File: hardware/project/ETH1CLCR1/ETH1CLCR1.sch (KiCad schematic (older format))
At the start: 0 parts

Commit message: Changes in schematics.
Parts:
- added M101: 60817-096, ETH1CLCR1:60817-096, symbol ETH1CLCR1:60817-096
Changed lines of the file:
@@
 S 2350 8200 1100 1500
 U 5E314C16
-F0 "FGEN Buffer" 50
+F0 "FGEN Buffer + Source resistor" 50
 F1 "FGEN_Buffer.sch" 50
 F2 "FGEN" I R 3450 9500 50
@@
 Wire Wire Line
 	11500 2350 12250 2350
+$Comp
+L ETH1CLCR1:60817-096 M101
+U 1 1 5E5B3C06
+P 800 10700
+F 0 "M101" H 1128 11046 50  0000 L CNN
+F 1 "60817-096" H 1128 10955 50  0000 L CNN
+F 2 "ETH1CLCR1:60817-096" H 800 10700 50  0001 C CNN
+F 3 "" H 800 10700 50  0001 C CNN
+	1    800  10700
+	1    0    0    -1
+$EndComp
 $EndSCHEMATC

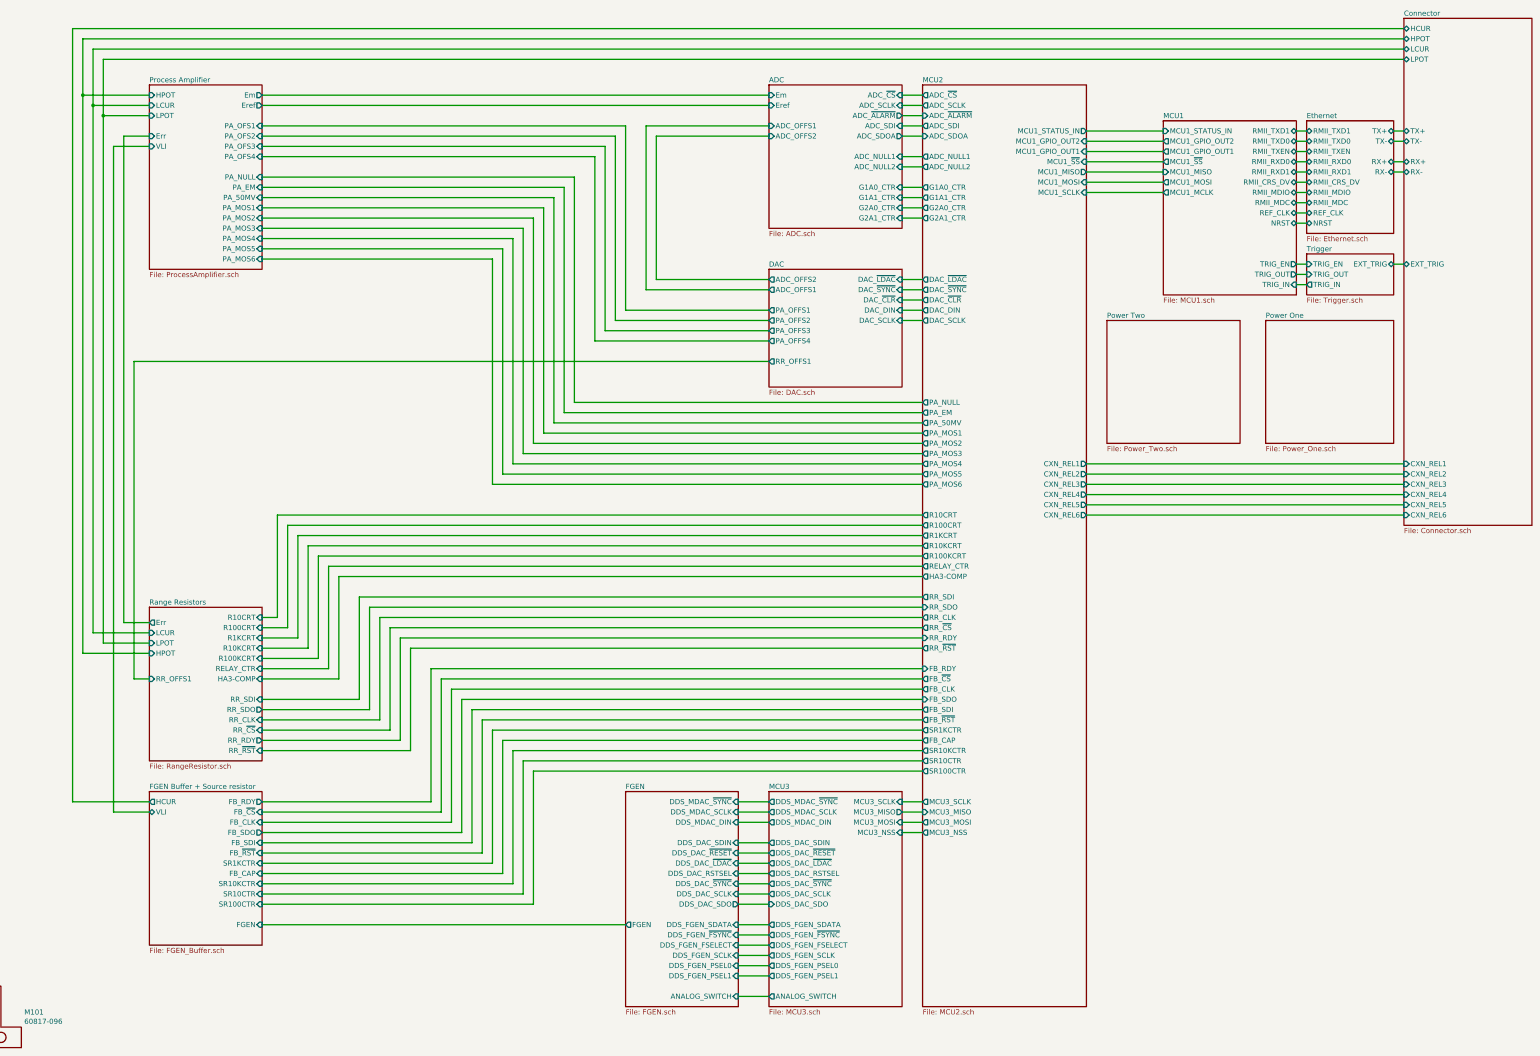
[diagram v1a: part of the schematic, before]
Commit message: Checked the schematics. Created BOM.
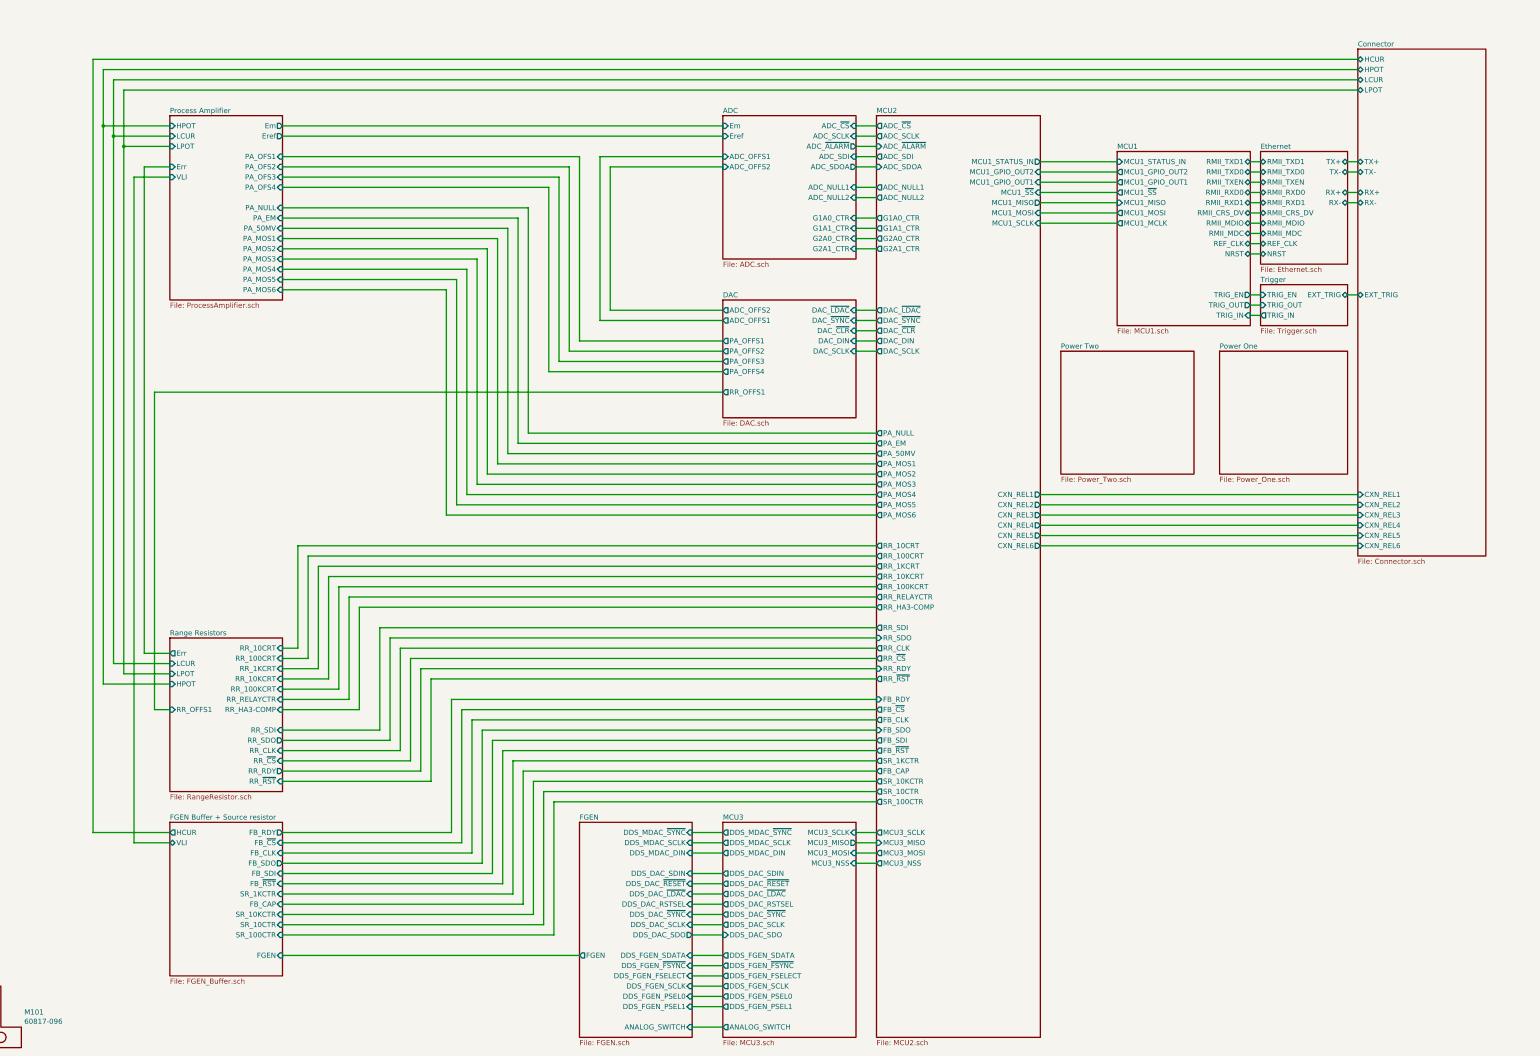
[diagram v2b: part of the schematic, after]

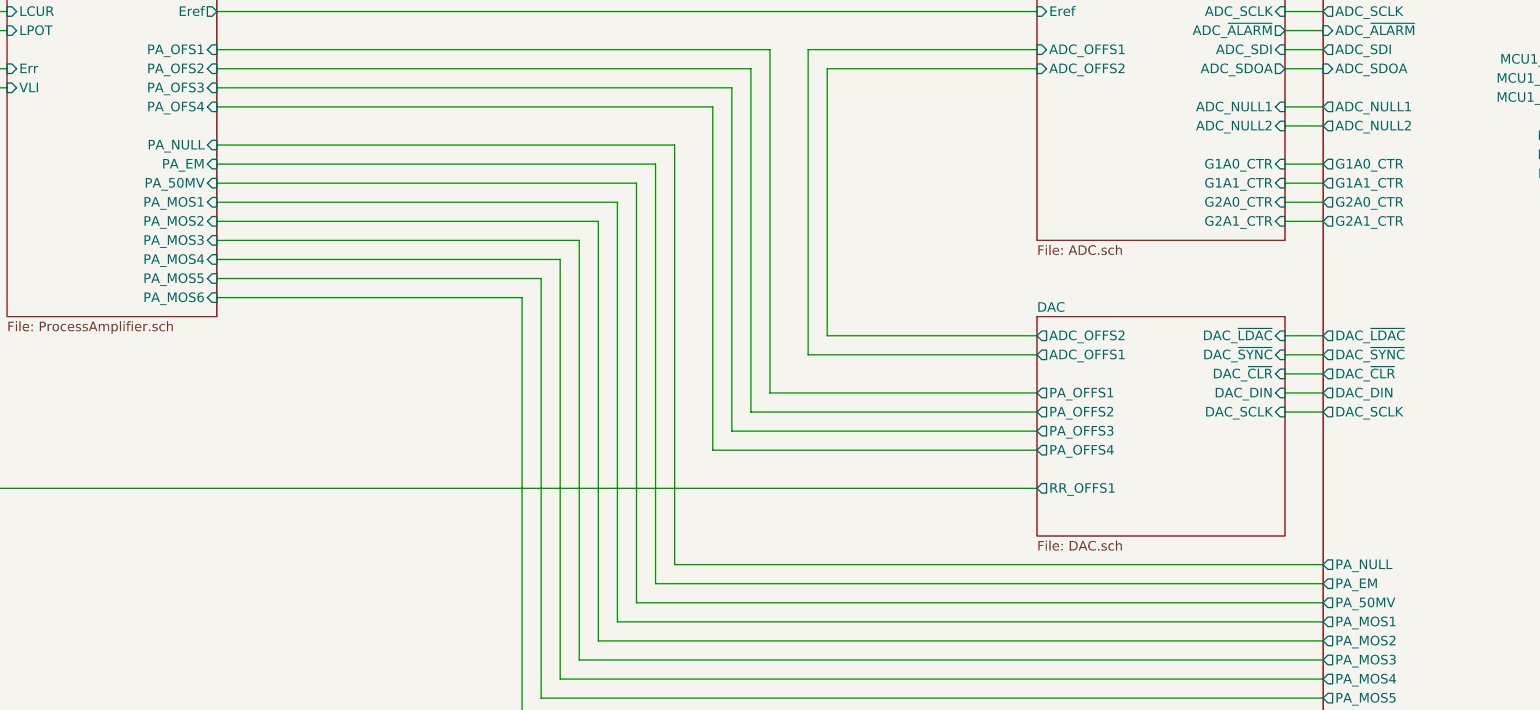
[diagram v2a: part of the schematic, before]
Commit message: Fixed some mistakes in the foorpeints. BOM list ready.
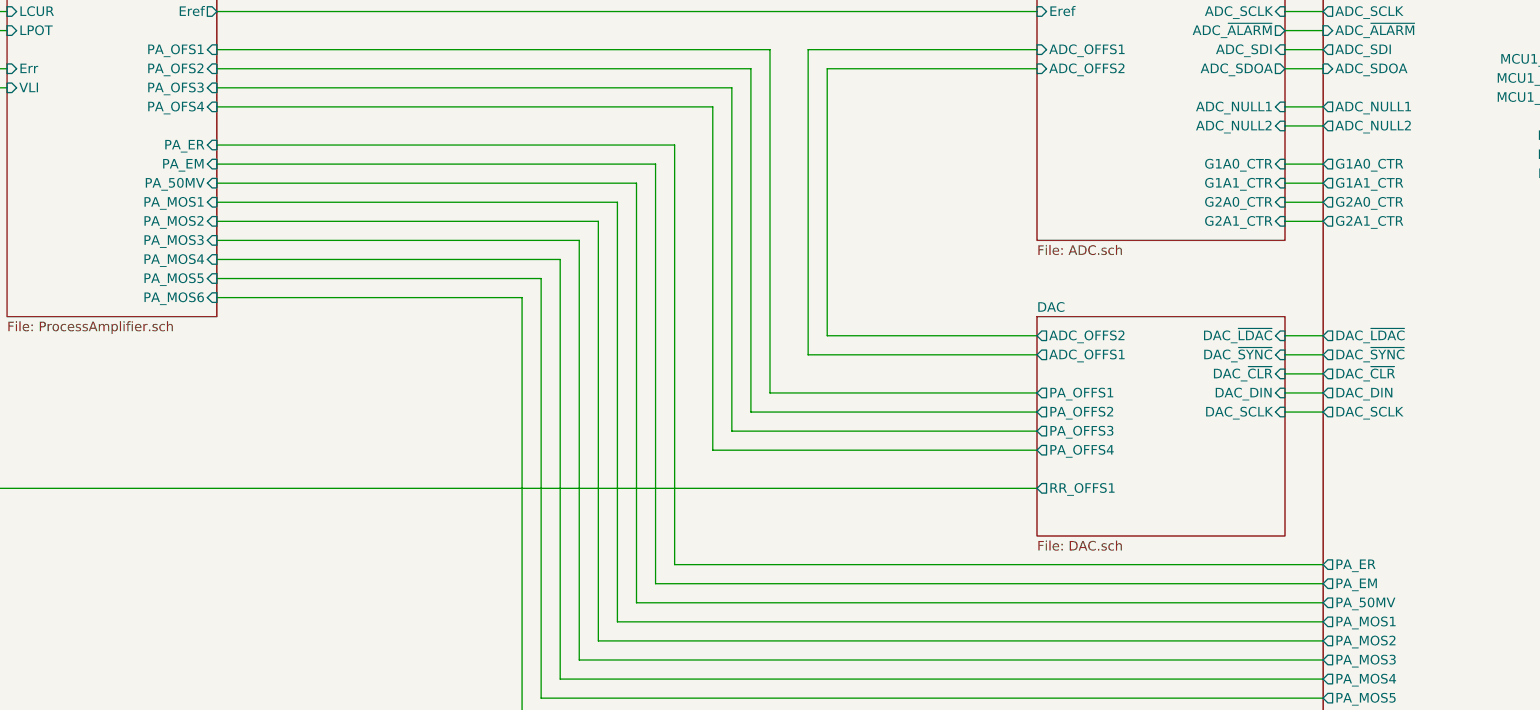
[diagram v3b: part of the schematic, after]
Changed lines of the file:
@@
 F11 "Eref" O R 3650 1800 50
 F12 "LPOT" I L 2550 1900 50
-F13 "PA_NULL" I R 3650 2500 50
+F13 "PA_ER" I R 3650 2500 50
 F14 "PA_EM" I R 3650 2600 50
 F15 "PA_50MV" I R 3650 2700 50
@@
 F18 "RR_RELAYCTR" O L 9450 6300 50
 F19 "RR_HA3-COMP" O L 9450 6400 50
-F20 "PA_NULL" O L 9450 4700 50
+F20 "PA_ER" O L 9450 4700 50
 F21 "PA_EM" O L 9450 4800 50
 F22 "PA_50MV" O L 9450 4900 50

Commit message: PCB layout
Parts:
- removed M101: 60817-096, ETH1CLCR1:60817-096, symbol ETH1CLCR1:60817-096
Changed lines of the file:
@@
 Wire Wire Line
 	11050 2650 11800 2650
-$Comp
-L ETH1CLCR1:60817-096 M101
-U 1 1 5E5B3C06
-P 800 10700
-F 0 "M101" H 1128 11046 50  0000 L CNN
-F 1 "60817-096" H 1128 10955 50  0000 L CNN
-F 2 "ETH1CLCR1:60817-096" H 800 10700 50  0001 C CNN
-F 3 "" H 800 10700 50  0001 C CNN
-	1    800  10700
-	1    0    0    -1
-$EndComp
 Wire Wire Line
 	1800 8600 2550 8600

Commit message: PCB layout
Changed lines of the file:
@@
 F13 "TRIG_OUT" O R 13100 3450 50
 F14 "TRIG_IN" I R 13100 3550 50
-F15 "MCU1_STATUS_IN" I L 11800 2050 50
-F16 "MCU1_GPIO_OUT2" O L 11800 2150 50
-F17 "MCU1_GPIO_OUT1" O L 11800 2250 50
-F18 "MCU1_~SS" O L 11800 2350 50
-F19 "MCU1_MISO" I L 11800 2450 50
-F20 "MCU1_MOSI" O L 11800 2550 50
-F21 "MCU1_MCLK" O L 11800 2650 50
+F15 "MCU1_GPIO_OUT2" O L 11800 2050 50
+F16 "MCU1_GPIO_OUT1" O L 11800 2150 50
+F17 "MCU1_~SS" O L 11800 2250 50
+F18 "MCU1_MISO" I L 11800 2350 50
+F19 "MCU1_MOSI" O L 11800 2450 50
+F20 "MCU1_MCLK" O L 11800 2550 50
+F21 "MCU1_STATUS_IN1" I L 11800 2650 50
+F22 "MCU1_STATUS_IN2" I L 11800 2750 50
 $EndSheet
 $Sheet
@@
 F59 "ADC_~ALARM" I L 9450 1900 50
 F60 "ADC_SDOA" I L 9450 2100 50
-F61 "MCU1_~SS" I R 11050 2350 50
-F62 "MCU1_MISO" O R 11050 2450 50
-F63 "MCU1_MOSI" I R 11050 2550 50
-F64 "MCU1_SCLK" I R 11050 2650 50
-F65 "MCU1_GPIO_OUT1" I R 11050 2250 50
-F66 "MCU1_STATUS_IN" O R 11050 2050 50
-F67 "MCU1_GPIO_OUT2" I R 11050 2150 50
+F61 "MCU1_~SS" I R 11050 2250 50
+F62 "MCU1_MISO" O R 11050 2350 50
+F63 "MCU1_MOSI" I R 11050 2450 50
+F64 "MCU1_SCLK" I R 11050 2550 50
+F65 "MCU1_GPIO_OUT1" I R 11050 2150 50
+F66 "MCU1_STATUS_IN1" O R 11050 2650 50
+F67 "MCU1_GPIO_OUT2" I R 11050 2050 50
+F68 "MCU1_STATUS_IN2" O R 11050 2750 50
 $EndSheet
 Wire Wire Line
@@
 $EndSheet
 Wire Wire Line
-	11050 2050 11800 2050
-Wire Wire Line
-	11050 2150 11800 2150
-Wire Wire Line
-	11050 2250 11800 2250
-Wire Wire Line
-	11050 2350 11800 2350
-Wire Wire Line
-	11050 2450 11800 2450
-Wire Wire Line
-	11050 2550 11800 2550
-Wire Wire Line
-	11050 2650 11800 2650
-Wire Wire Line
 	1800 8600 2550 8600
 Wire Wire Line
@@
 Wire Wire Line
 	2300 6850 2300 2100
+Wire Wire Line
+	11050 2550 11800 2550
+Wire Wire Line
+	11050 2450 11800 2450
+Wire Wire Line
+	11050 2350 11800 2350
+Wire Wire Line
+	11050 2250 11800 2250
+Wire Wire Line
+	11050 2150 11800 2150
+Wire Wire Line
+	11050 2050 11800 2050
+Wire Wire Line
+	11050 2650 11800 2650
+Wire Wire Line
+	11050 2750 11800 2750
 $EndSCHEMATC

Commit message: Was able to set the SPI3 (MCU2) to run with 80 MHZ clock speed with AD7380. Using HAL lib for SPI and GPIO, too slow switching. Need to change to LL with DMA.
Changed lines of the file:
@@
 F0 "Range Resistors" 50
 F1 "RangeResistor.sch" 50
-F2 "RR_1KCRT" I R 3650 7000 50
-F3 "RR_10KCRT" I R 3650 7100 50
-F4 "RR_100CRT" I R 3650 6900 50
-F5 "RR_10CRT" I R 3650 6800 50
-F6 "RR_100KCRT" I R 3650 7200 50
+F2 "RR_1KCTR" I R 3650 7000 50
+F3 "RR_10KCTR" I R 3650 7100 50
+F4 "RR_100CTR" I R 3650 6900 50
+F5 "RR_10CTR" I R 3650 6800 50
+F6 "RR_100KCTR" I R 3650 7200 50
 F7 "Err" O L 2550 6850 50
 F8 "RR_RELAYCTR" I R 3650 7300 50
@@
 F11 "CXN_REL2" O R 11050 5400 50
 F12 "CXN_REL3" O R 11050 5500 50
-F13 "RR_100CRT" O L 9450 5900 50
-F14 "RR_10CRT" O L 9450 5800 50
-F15 "RR_1KCRT" O L 9450 6000 50
-F16 "RR_10KCRT" O L 9450 6100 50
-F17 "RR_100KCRT" O L 9450 6200 50
+F13 "RR_100CTR" O L 9450 5900 50
+F14 "RR_10CTR" O L 9450 5800 50
+F15 "RR_1KCTR" O L 9450 6000 50
+F16 "RR_10KCTR" O L 9450 6100 50
+F17 "RR_100KCTR" O L 9450 6200 50
 F18 "RR_RELAYCTR" O L 9450 6300 50
 F19 "RR_HA3-COMP" O L 9450 6400 50
